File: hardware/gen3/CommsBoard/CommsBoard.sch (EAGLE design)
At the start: 54 parts, among them U1 ATMEGA165PV-8AU

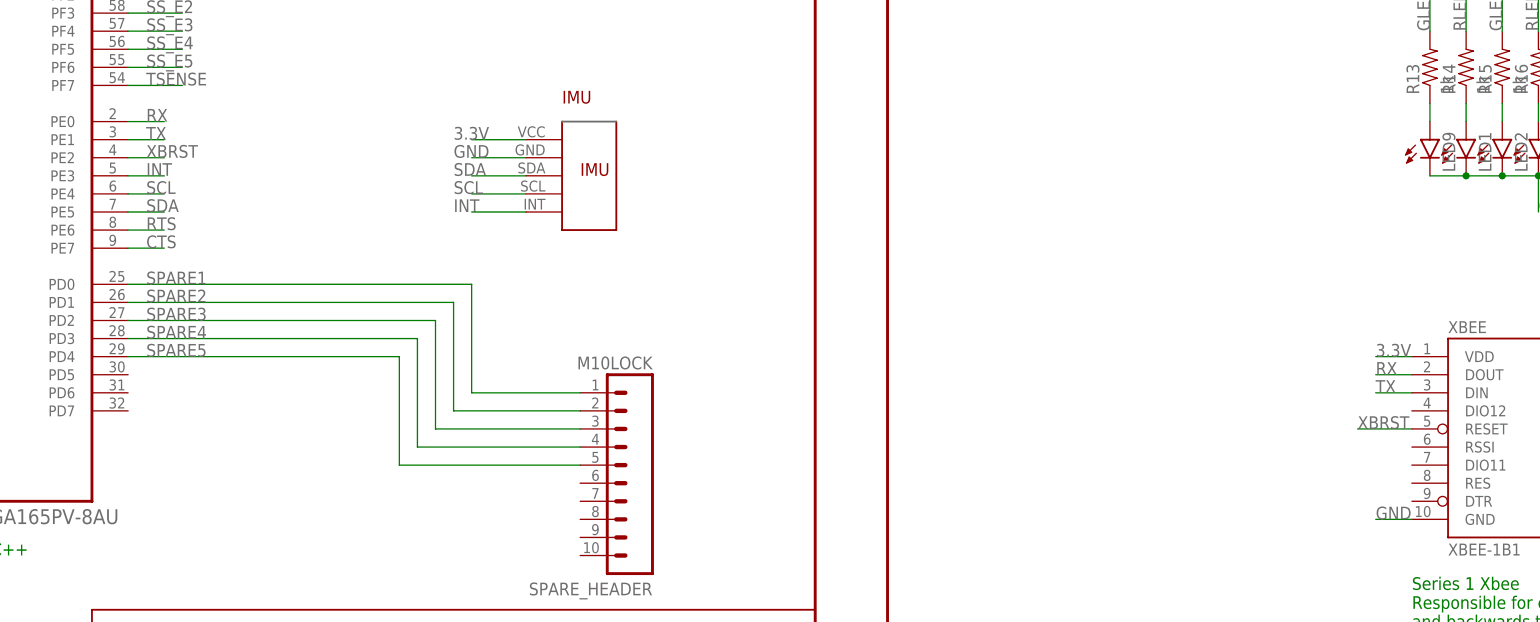
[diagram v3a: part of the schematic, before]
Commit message: xbee reset button added
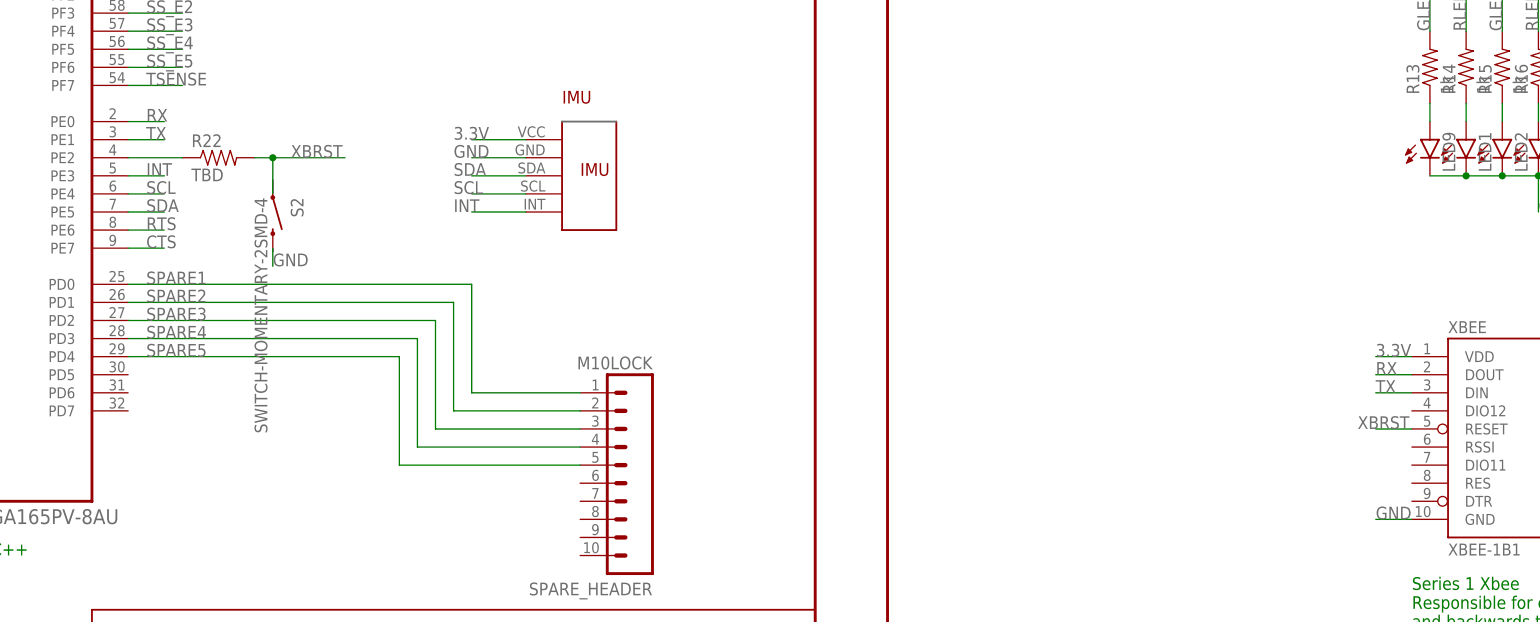
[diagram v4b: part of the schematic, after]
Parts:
- added R22: TBD, SparkFun-Passives:RESISTOR0805-RES
- added S2: SWITCH-MOMENTARY-2SMD-4, SparkFun-Electromechanical:SWITCH-MOMENTARY-2SMD-4
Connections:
- new net N$2: R22.1, U1.PE2
- net XBRST: now also R22.2; no longer U1.PE2
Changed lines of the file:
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@@
 <part name="C10" library="SparkFun-Capacitors" deviceset="CAP" device="0805" value="1uF"/>
 <part name="U$3" library="gen3" deviceset="LOGO" device=""/>
+<part name="R22" library="SparkFun-Passives" deviceset="RESISTOR" device="0805-RES" value="TBD"/>
+<part name="S2" library="SparkFun-Electromechanical" deviceset="SWITCH-MOMENTARY-2" device="SMD-4"/>
 </parts>
 <sheets>
@@
 <instance part="C10" gate="G$1" x="109.22" y="167.64" rot="R90"/>
 <instance part="U$3" gate="G$1" x="25.4" y="127"/>
+<instance part="R22" gate="G$1" x="165.1" y="99.06"/>
+<instance part="S2" gate="G$1" x="172.72" y="90.932" rot="R270"/>
 </instances>
 <busses>
@@
 <label x="111.76" y="170.18" size="1.778" layer="95"/>
 </segment>
+<segment>
+<wire x1="172.72" y1="86.36" x2="172.72" y2="83.82" width="0.1524" layer="91"/>
+<label x="172.72" y="83.82" size="1.778" layer="95"/>
+</segment>
 </net>
 <net name="3.3V" class="0">
@@
 </segment>
 </net>
-<net name="XBRST" class="0">
-<segment>
-<pinref part="XBEE" gate="G$1" pin="RESET"/>
-<wire x1="332.74" y1="60.96" x2="325.12" y2="60.96" width="0.1524" layer="91"/>
-<label x="325.12" y="60.96" size="1.778" layer="95"/>
-</segment>
-<segment>
-<wire x1="152.4" y1="99.06" x2="157.48" y2="99.06" width="0.1524" layer="91"/>
-<label x="154.94" y="99.06" size="1.778" layer="95"/>
-<pinref part="U1" gate="A" pin="PE2"/>
-</segment>
-</net>
 <net name="N$17" class="0">
 <segment>
@@
 </segment>
 </net>
+<net name="N$2" class="0">
+<segment>
+<pinref part="U1" gate="A" pin="PE2"/>
+<pinref part="R22" gate="G$1" pin="1"/>
+<wire x1="152.4" y1="99.06" x2="160.02" y2="99.06" width="0.1524" layer="91"/>
+</segment>
+</net>
+<net name="XBRST" class="0">
+<segment>
+<pinref part="R22" gate="G$1" pin="2"/>
+<wire x1="170.18" y1="99.06" x2="172.72" y2="99.06" width="0.1524" layer="91"/>
+<label x="175.26" y="99.06" size="1.778" layer="95"/>
+<wire x1="172.72" y1="99.06" x2="182.88" y2="99.06" width="0.1524" layer="91"/>
+<wire x1="172.72" y1="93.98" x2="172.72" y2="99.06" width="0.1524" layer="91"/>
+<junction x="172.72" y="99.06"/>
+</segment>
+<segment>
+<pinref part="XBEE" gate="G$1" pin="RESET"/>
+<wire x1="332.74" y1="60.96" x2="327.66" y2="60.96" width="0.1524" layer="91"/>
+<label x="325.12" y="60.96" size="1.778" layer="95"/>
+</segment>
+</net>

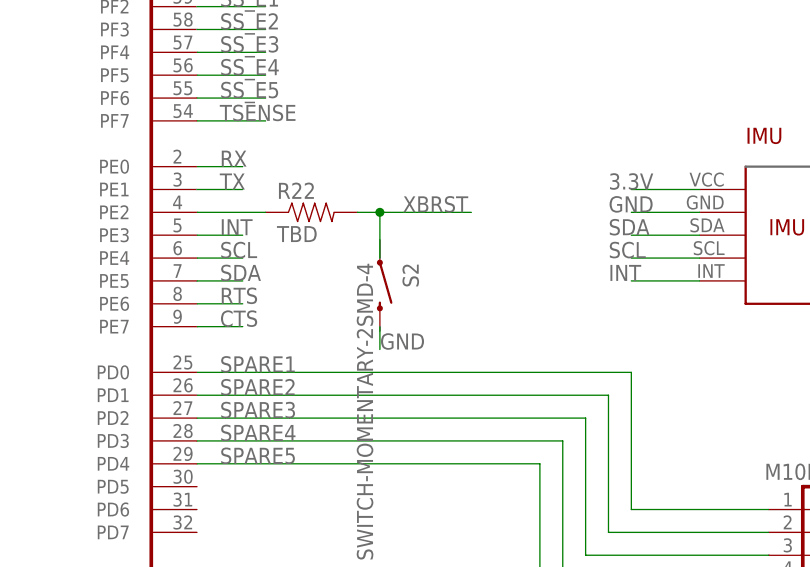
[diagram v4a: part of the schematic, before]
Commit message: fixing board with new switch
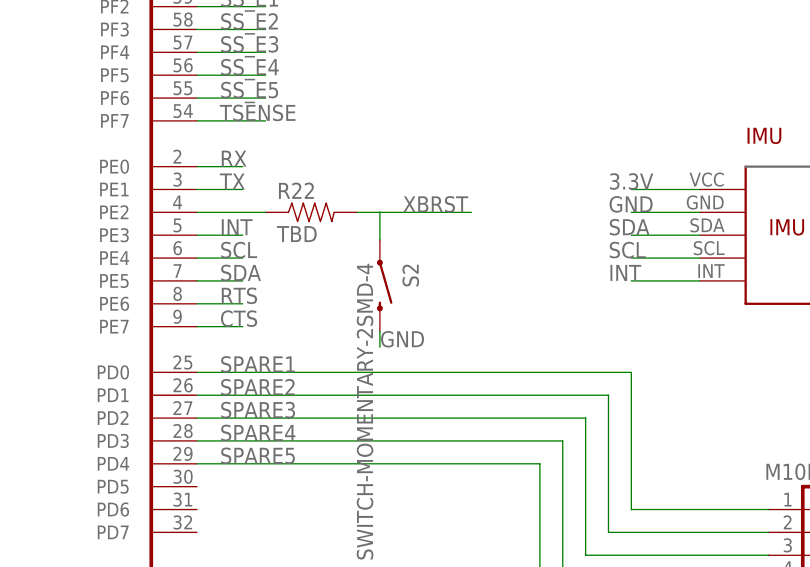
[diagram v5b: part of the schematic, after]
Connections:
- net GND: now also S2.2
- net XBRST: now also S2.1
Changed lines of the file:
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@@
 <setting verticaltext="up"/>
 </settings>
-<grid distance="0.1" unitdist="inch" unit="inch" style="lines" multiple="1" display="no" altdistance="0.01" altunitdist="inch" altunit="inch"/>
+<grid distance="0.01" unitdist="inch" unit="inch" style="lines" multiple="1" display="no" altdistance="0.01" altunitdist="inch" altunit="inch"/>
 <layers>
 <layer number="1" name="Top" color="4" fill="1" visible="no" active="no"/>
@@
 </segment>
 <segment>
-<wire x1="172.72" y1="86.36" x2="172.72" y2="83.82" width="0.1524" layer="91"/>
-<label x="172.72" y="83.82" size="1.778" layer="95"/>
+<pinref part="S2" gate="G$1" pin="2"/>
+<wire x1="172.72" y1="85.852" x2="172.72" y2="84.074" width="0.1524" layer="91"/>
+<label x="172.72" y="84.074" size="1.778" layer="95"/>
 </segment>
 </net>
@@
 <segment>
 <pinref part="R22" gate="G$1" pin="2"/>
+<label x="175.26" y="99.06" size="1.778" layer="95"/>
 <wire x1="170.18" y1="99.06" x2="172.72" y2="99.06" width="0.1524" layer="91"/>
-<label x="175.26" y="99.06" size="1.778" layer="95"/>
+<pinref part="S2" gate="G$1" pin="1"/>
 <wire x1="172.72" y1="99.06" x2="182.88" y2="99.06" width="0.1524" layer="91"/>
-<wire x1="172.72" y1="93.98" x2="172.72" y2="99.06" width="0.1524" layer="91"/>
-<junction x="172.72" y="99.06"/>
-</segment>
-<segment>
+<wire x1="172.72" y1="96.012" x2="172.72" y2="99.06" width="0.1524" layer="91"/>
+</segment>
+<segment>

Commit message: edits to comms
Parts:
- C3, C4: value 100uF -> 47uF; device gen3:CAP-POLAR -> SparkFun-Capacitors:CAP1206
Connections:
- net 3.3V: now also C3.1; no longer C3.+
- net 5V: now also C4.1; no longer C4.+
- net GND: now also C3.2, C4.2; no longer C3.-, C4.-
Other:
- moved on the sheet: S2

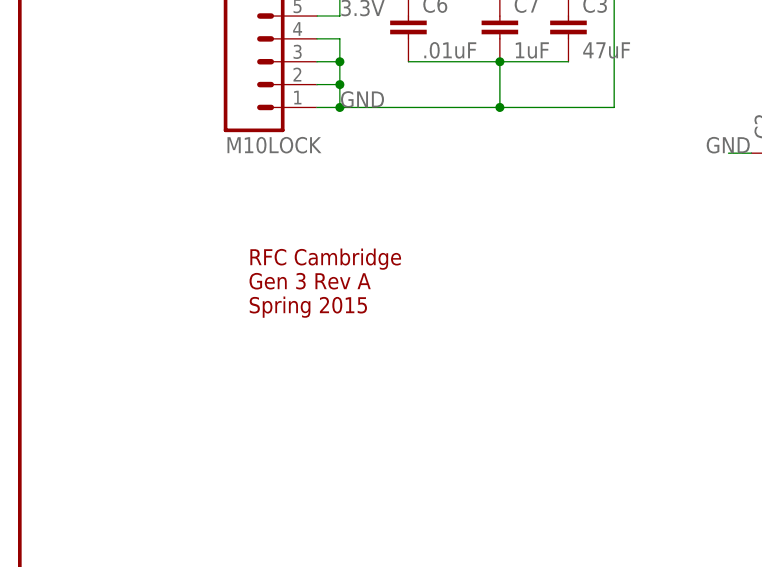
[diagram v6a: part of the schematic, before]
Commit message: nice silkscreen for comms
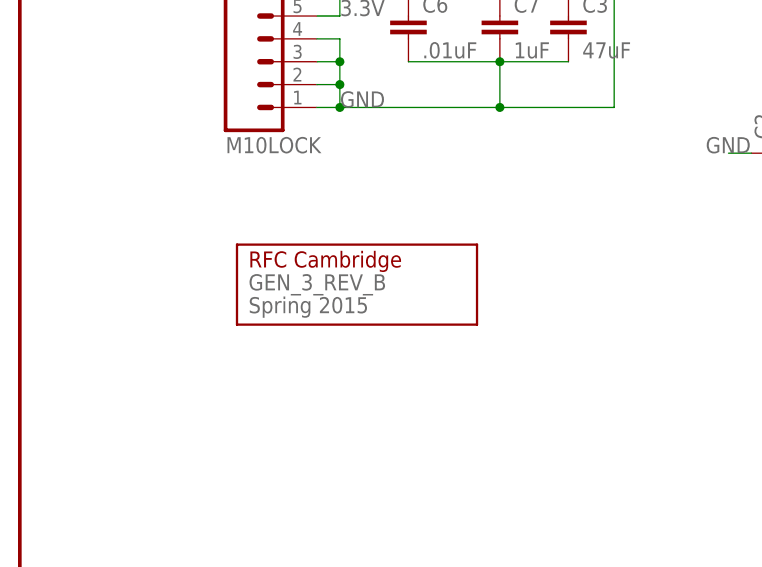
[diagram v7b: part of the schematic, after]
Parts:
- GEN_3_REV_B: value LOGO -> Spring 2015
- renumbered U$3 to GEN_3_REV_B
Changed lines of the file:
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@@
 <setting verticaltext="up"/>
 </settings>
-<grid distance="0.1" unitdist="inch" unit="inch" style="lines" multiple="1" display="yes" altdistance="0.01" altunitdist="inch" altunit="inch"/>
+<grid distance="0.1" unitdist="inch" unit="inch" style="lines" multiple="1" display="no" altdistance="0.01" altunitdist="inch" altunit="inch"/>
 <layers>
-<layer number="1" name="Top" color="4" fill="1" visible="yes" active="no"/>
-<layer number="2" name="Route2" color="1" fill="3" visible="yes" active="no"/>
-<layer number="3" name="Route3" color="4" fill="3" visible="yes" active="no"/>
-<layer number="14" name="Route14" color="1" fill="6" visible="yes" active="no"/>
-<layer number="15" name="Route15" color="4" fill="6" visible="yes" active="no"/>
-<layer number="16" name="Bottom" color="1" fill="1" visible="yes" active="no"/>
-<layer number="17" name="Pads" color="2" fill="1" visible="yes" active="no"/>
-<layer number="18" name="Vias" color="2" fill="1" visible="yes" active="no"/>
-<layer number="19" name="Unrouted" color="6" fill="1" visible="yes" active="no"/>
-<layer number="20" name="Dimension" color="15" fill="1" visible="yes" active="no"/>
-<layer number="21" name="tPlace" color="16" fill="1" visible="yes" active="no"/>
-<layer number="22" name="bPlace" color="14" fill="1" visible="yes" active="no"/>
-<layer number="23" name="tOrigins" color="15" fill="1" visible="yes" active="no"/>
-<layer number="24" name="bOrigins" color="15" fill="1" visible="yes" active="no"/>
-<layer number="25" name="tNames" color="7" fill="1" visible="yes" active="no"/>
-<layer number="26" name="bNames" color="7" fill="1" visible="yes" active="no"/>
-<layer number="27" name="tValues" color="7" fill="1" visible="yes" active="no"/>
-<layer number="28" name="bValues" color="7" fill="1" visible="yes" active="no"/>
+<layer number="1" name="Top" color="4" fill="1" visible="no" active="no"/>
+<layer number="2" name="Route2" color="1" fill="3" visible="no" active="no"/>
+<layer number="3" name="Route3" color="4" fill="3" visible="no" active="no"/>
+<layer number="14" name="Route14" color="1" fill="6" visible="no" active="no"/>
+<layer number="15" name="Route15" color="4" fill="6" visible="no" active="no"/>
+<layer number="16" name="Bottom" color="1" fill="1" visible="no" active="no"/>
+<layer number="17" name="Pads" color="2" fill="1" visible="no" active="no"/>
+<layer number="18" name="Vias" color="2" fill="1" visible="no" active="no"/>
+<layer number="19" name="Unrouted" color="6" fill="1" visible="no" active="no"/>
+<layer number="20" name="Dimension" color="15" fill="1" visible="no" active="no"/>
+<layer number="21" name="tPlace" color="16" fill="1" visible="no" active="no"/>
+<layer number="22" name="bPlace" color="14" fill="1" visible="no" active="no"/>
+<layer number="23" name="tOrigins" color="15" fill="1" visible="no" active="no"/>
+<layer number="24" name="bOrigins" color="15" fill="1" visible="no" active="no"/>
+<layer number="25" name="tNames" color="7" fill="1" visible="no" active="no"/>
+<layer number="26" name="bNames" color="7" fill="1" visible="no" active="no"/>
+<layer number="27" name="tValues" color="7" fill="1" visible="no" active="no"/>
+<layer number="28" name="bValues" color="7" fill="1" visible="no" active="no"/>
 <layer number="29" name="tStop" color="7" fill="3" visible="no" active="no"/>
 <layer number="30" name="bStop" color="7" fill="6" visible="no" active="no"/>
@@
 <layer number="35" name="tGlue" color="7" fill="4" visible="no" active="no"/>
 <layer number="36" name="bGlue" color="7" fill="5" visible="no" active="no"/>
-<layer number="37" name="tTest" color="7" fill="1" visible="yes" active="no"/>
-<layer number="38" name="bTest" color="7" fill="1" visible="yes" active="no"/>
+<layer number="37" name="tTest" color="7" fill="1" visible="no" active="no"/>
+<layer number="38" name="bTest" color="7" fill="1" visible="no" active="no"/>
 <layer number="39" name="tKeepout" color="4" fill="11" visible="no" active="no"/>
 <layer number="40" name="bKeepout" color="1" fill="11" visible="no" active="no"/>
@@
 <layer number="44" name="Drills" color="7" fill="1" visible="no" active="no"/>
 <layer number="45" name="Holes" color="7" fill="1" visible="no" active="no"/>
-<layer number="46" name="Milling" color="3" fill="1" visible="yes" active="no"/>
-<layer number="47" name="Measures" color="7" fill="1" visible="yes" active="no"/>
-<layer number="48" name="Document" color="7" fill="1" visible="yes" active="no"/>
-<layer number="49" name="Reference" color="7" fill="1" visible="yes" active="no"/>
-<layer number="50" name="dxf" color="7" fill="1" visible="yes" active="no"/>
-<layer number="51" name="tDocu" color="6" fill="1" visible="yes" active="no"/>
-<layer number="52" name="bDocu" color="7" fill="1" visible="yes" active="no"/>
-<layer number="53" name="tGND_GNDA" color="7" fill="9" visible="yes" active="no"/>
-<layer number="54" name="bGND_GNDA" color="1" fill="9" visible="yes" active="no"/>
-<layer number="56" name="wert" color="7" fill="1" visible="yes" active="no"/>
-<layer number="57" name="tCAD" color="7" fill="1" visible="yes" active="no"/>
-<layer number="59" name="tCarbon" color="7" fill="1" visible="yes" active="no"/>
-<layer number="60" name="bCarbon" color="7" fill="1" visible="yes" active="no"/>
+<layer number="46" name="Milling" color="3" fill="1" visible="no" active="no"/>
+<layer number="47" name="Measures" color="7" fill="1" visible="no" active="no"/>
+<layer number="48" name="Document" color="7" fill="1" visible="no" active="no"/>
+<layer number="49" name="Reference" color="7" fill="1" visible="no" active="no"/>
+<layer number="50" name="dxf" color="7" fill="1" visible="no" active="no"/>
+<layer number="51" name="tDocu" color="6" fill="1" visible="no" active="no"/>
+<layer number="52" name="bDocu" color="7" fill="1" visible="no" active="no"/>
+<layer number="53" name="tGND_GNDA" color="7" fill="9" visible="no" active="no"/>
+<layer number="54" name="bGND_GNDA" color="1" fill="9" visible="no" active="no"/>
+<layer number="56" name="wert" color="7" fill="1" visible="no" active="no"/>
+<layer number="57" name="tCAD" color="7" fill="1" visible="no" active="no"/>
+<layer number="59" name="tCarbon" color="7" fill="1" visible="no" active="no"/>
+<layer number="60" name="bCarbon" color="7" fill="1" visible="no" active="no"/>
 <layer number="90" name="Modules" color="5" fill="1" visible="yes" active="yes"/>
 <layer number="91" name="Nets" color="2" fill="1" visible="yes" active="yes"/>
@@
 <part name="C9" library="SparkFun-Capacitors" deviceset="CAP" device="0805" value=".01uF"/>
 <part name="C10" library="SparkFun-Capacitors" deviceset="CAP" device="0805" value="1uF"/>
-<part name="U$3" library="gen3" deviceset="LOGO" device=""/>
+<part name="GEN_3_REV_B" library="gen3" deviceset="LOGO" device="" value="Spring 2015"/>
 <part name="R22" library="SparkFun-Passives" deviceset="RESISTOR" device="0805-RES" value="TBD"/>
 <part name="S2" library="SparkFun-Electromechanical" deviceset="SWITCH-MOMENTARY-2" device="SMD-4"/>
@@
 <instance part="C9" gate="G$1" x="109.22" y="157.48" rot="R90"/>
 <instance part="C10" gate="G$1" x="109.22" y="167.64" rot="R90"/>
-<instance part="U$3" gate="G$1" x="25.4" y="127"/>
+<instance part="GEN_3_REV_B" gate="G$1" x="25.4" y="127"/>
 <instance part="R22" gate="G$1" x="165.1" y="99.06"/>
 <instance part="S2" gate="G$1" x="172.72" y="91.44" rot="R270"/>

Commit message: cleared some kicker
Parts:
- added C11: .01uF, SparkFun-Capacitors:CAP0805
- added C12: 1uF, SparkFun-Capacitors:CAP0805
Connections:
- net 3.3V: now also C11.2, C12.2
- net GND: now also C11.1, C12.1
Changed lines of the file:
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@@
 <part name="C3" library="SparkFun-Capacitors" deviceset="CAP" device="1206" value="47uF"/>
 <part name="C4" library="SparkFun-Capacitors" deviceset="CAP" device="1206" value="47uF"/>
+<part name="C11" library="SparkFun-Capacitors" deviceset="CAP" device="0805" value=".01uF"/>
+<part name="C12" library="SparkFun-Capacitors" deviceset="CAP" device="0805" value="1uF"/>
 </parts>
 <sheets>
@@
 <instance part="C3" gate="G$1" x="60.96" y="157.48"/>
 <instance part="C4" gate="G$1" x="76.2" y="167.64"/>
+<instance part="C11" gate="G$1" x="325.12" y="76.2"/>
+<instance part="C12" gate="G$1" x="317.5" y="76.2"/>
 </instances>
 <busses>
@@
 <label x="172.72" y="84.074" size="1.778" layer="95"/>
 </segment>
+<segment>
+<pinref part="C12" gate="G$1" pin="1"/>
+<wire x1="317.5" y1="81.28" x2="317.5" y2="83.82" width="0.1524" layer="91"/>
+<wire x1="317.5" y1="83.82" x2="325.12" y2="83.82" width="0.1524" layer="91"/>
+<pinref part="C11" gate="G$1" pin="1"/>
+<wire x1="325.12" y1="83.82" x2="325.12" y2="81.28" width="0.1524" layer="91"/>
+<wire x1="317.5" y1="83.82" x2="309.88" y2="83.82" width="0.1524" layer="91"/>
+<junction x="317.5" y="83.82"/>
+<label x="309.88" y="83.82" size="1.778" layer="95"/>
+</segment>
 </net>
 <net name="3.3V" class="0">
@@
 <segment>
 <pinref part="XBEE" gate="G$1" pin="VDD"/>
-<wire x1="332.74" y1="71.12" x2="327.66" y2="71.12" width="0.1524" layer="91"/>
-<label x="327.66" y="71.12" size="1.778" layer="95"/>
-</segment>
-<segment>
+<wire x1="332.74" y1="71.12" x2="325.12" y2="71.12" width="0.1524" layer="91"/>
+<label x="309.88" y="71.12" size="1.778" layer="95"/>
+<pinref part="C12" gate="G$1" pin="2"/>
+<wire x1="325.12" y1="71.12" x2="317.5" y2="71.12" width="0.1524" layer="91"/>
+<wire x1="317.5" y1="71.12" x2="309.88" y2="71.12" width="0.1524" layer="91"/>
+<wire x1="317.5" y1="73.66" x2="317.5" y2="71.12" width="0.1524" layer="91"/>
+<junction x="317.5" y="71.12"/>
+<pinref part="C11" gate="G$1" pin="2"/>
+<wire x1="325.12" y1="73.66" x2="325.12" y2="71.12" width="0.1524" layer="91"/>
+<junction x="325.12" y="71.12"/>
+</segment>
+<segment>
